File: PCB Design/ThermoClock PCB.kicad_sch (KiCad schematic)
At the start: 39 parts, among them J1 Jack-DC, J10 Conn_01x07, J2 Conn_01x03, J3 Conn_01x07, J4 Conn_01x07, J5 Conn_01x07, J6 Conn_01x07, J7 Conn_01x07, J8 Conn_01x07, J9 Conn_01x07, P1 Power, P2 Analog, P3 Analog, P4 Digital, P5 PWM, P6 PWM, P7 Communication

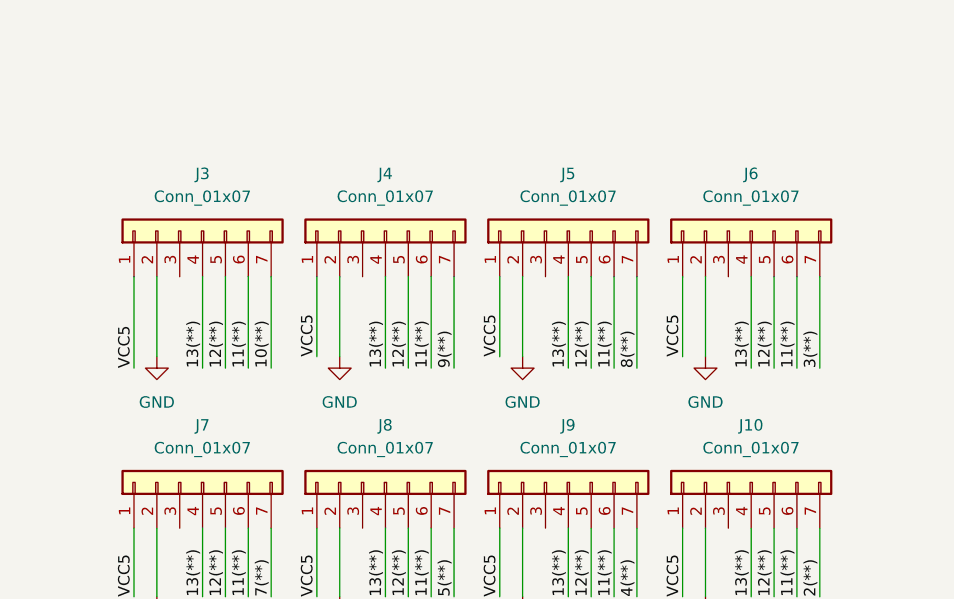
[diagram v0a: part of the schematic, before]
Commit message: sensor pin correction
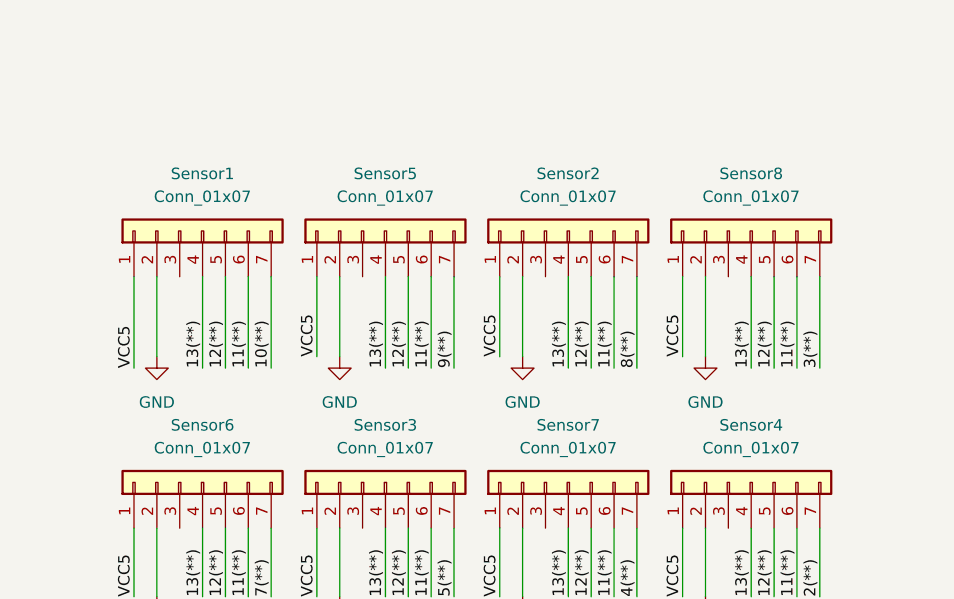
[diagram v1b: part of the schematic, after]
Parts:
- renumbered J3 to Sensor1, J5 to Sensor2, J8 to Sensor3, J10 to Sensor4, J4 to Sensor5, J7 to Sensor6, J9 to Sensor7, J6 to Sensor8
